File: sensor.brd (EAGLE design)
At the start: 64 x 64 mm, 27 parts, among them U1 NX1117C33Z, U2 NX1117CE50Z, U3 BMP180, U4 TSL2561

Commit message: Added some drill holes for mounting the PCB into a housing.
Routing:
- net N$2: track 25.7 -> 18.4 mm
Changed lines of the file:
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@@
 <wire x1="48.02125" y1="38.4575" x2="16.02125" y2="38.4575" width="0.254" layer="23"/>
 <wire x1="16.02125" y1="38.4575" x2="16.02125" y2="13.9575" width="0.254" layer="23"/>
+<hole x="3" y="32" drill="3.3"/>
+<hole x="61" y="32" drill="3.3"/>
 </plain>
 <attributes>
@@
 <contactref element="BAT2" pad="GND@1"/>
 <contactref element="BAT3" pad="PWR@1"/>
-<wire x1="57.146" y1="24" x2="62" y2="24" width="1.016" layer="1"/>
-<wire x1="62" y1="24" x2="62" y2="40" width="1.016" layer="1"/>
-<wire x1="62" y1="40" x2="57.146" y2="40" width="1.016" layer="1"/>
+<wire x1="57.146" y1="24" x2="58.34875" y2="24" width="1.016" layer="1"/>
+<wire x1="58.34875" y1="24" x2="58.34875" y2="40" width="1.016" layer="1"/>
+<wire x1="58.34875" y1="40" x2="57.146" y2="40" width="1.016" layer="1"/>
 </signal>
 <signal name="N$3">

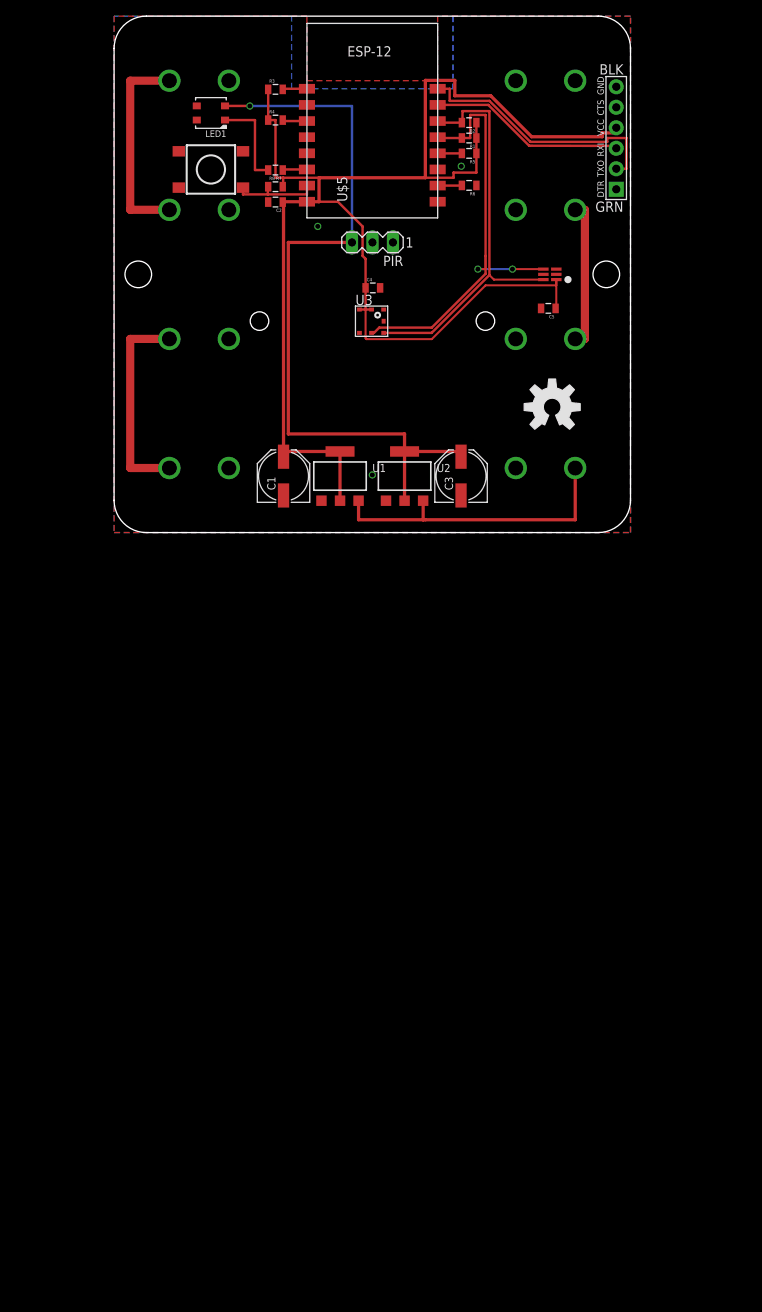
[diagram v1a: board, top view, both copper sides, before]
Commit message: lipo 18650 cell, TP4056 1A boost/charge controller
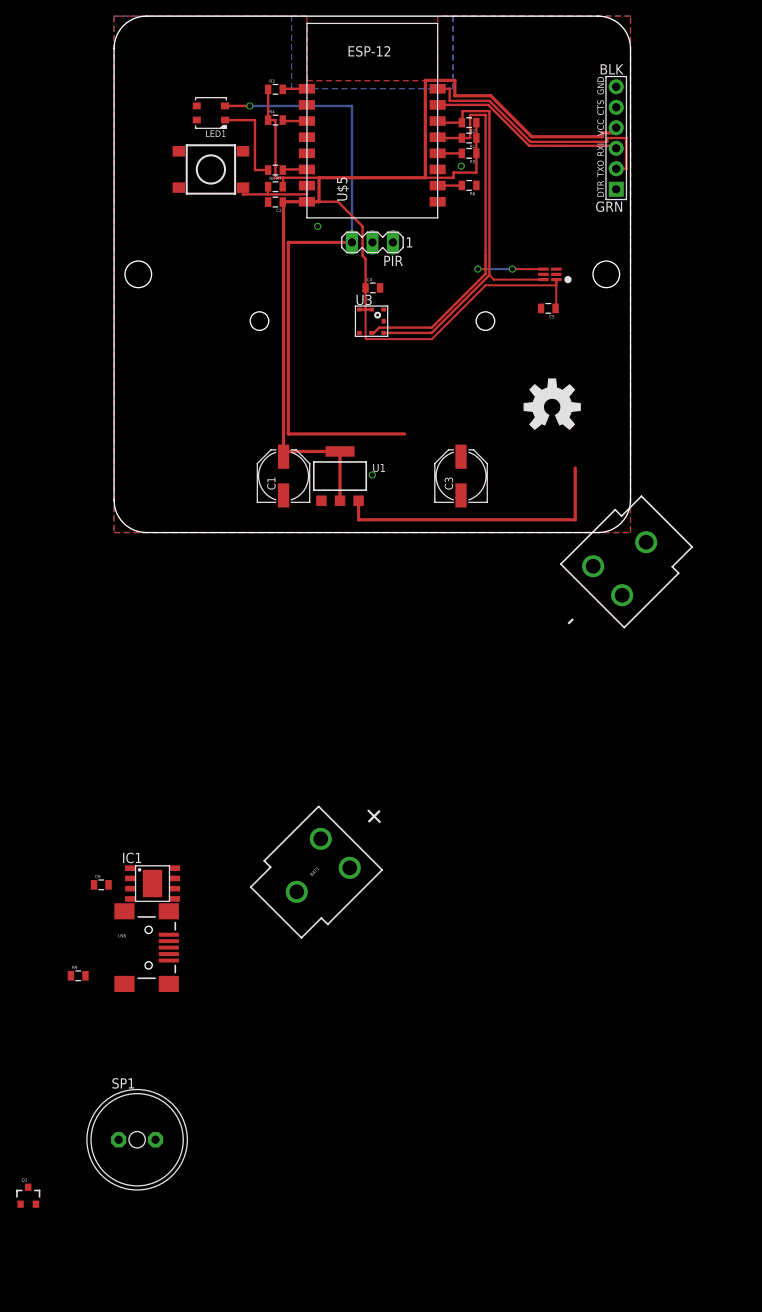
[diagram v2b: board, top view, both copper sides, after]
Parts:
- removed BAT2, BAT3, BAT4: (no value), SparkFun-Electromechanical:BATTERY-AA
- removed U2: NX1117CE50Z, nxp_60:SOT223
- added C6: 10uf, SparkFun-Capacitors:0805
- added IC1: TP4056, TP4056:SOP-8
- added Q1: (no value), SparkFun-DiscreteSemi:SOT23-3
- added R9: 122, SparkFun-Resistors:0805
- added SP1: SPEAKER/AL11P, adafruit:AL11P
- added U$6: USB-MINIB-5PIN, SparkFun-Connectors:USB-MINIB
- BAT1: device SparkFun-Electromechanical:BATTERY-AA -> SparkFun-Electromechanical:BATTERY_18650-HOLDER
- moved BAT1 33.2 mm to (44.3, -22.9), flipped to the top, turned to 45 degrees
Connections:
- removed net N$1: BAT1.GND@1, BAT2.PWR@1
- new net N$6: Q1.2, SP1.+
- new net SPKR: Q1.1
- new net USB_D+: U$6.D+
- new net USB_D-: U$6.D-
- net 5V: now also IC1.4, IC1.8, Q1.3, U$6.VBUS; no longer U2.2, U2.4
- net GND: now also BAT1.GND@1, C6.2, SP1.-, U$6.GND, U$6.MTN1, U$6.MTN2, U$6.MTN3, U$6.MTN4; no longer BAT4.GND@1, U2.1
- net N$2: now also IC1.1, IC1.3, R9.1; no longer BAT2.GND@1, BAT3.PWR@1
- net N$3: now also IC1.2, R9.2; no longer BAT3.GND@1, BAT4.PWR@1
- net V_BATT: now also C6.1, IC1.5; no longer U2.3
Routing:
- net N$3: track 25.7 -> 0.00 mm
- net N$1: track 25.7 -> 0.00 mm
- net N$2: track 18.4 -> 0.00 mm
- net 5V: track 94.6 -> 79.3 mm
- net V_BATT: track 38.0 -> 35.6 mm
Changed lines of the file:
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@@
 <attribute name="VOLTAGE" value="5.0V" x="28" y="7" size="1.778" layer="27" display="off"/>
 </element>
-<element name="U2" library="nxp_60" package="SOT223" value="NX1117CE50Z" x="36" y="7">
-<attribute name="TOLERANCE" value="1.25%" x="36" y="7" size="1.778" layer="27" display="off"/>
-<attribute name="12NC" value="" x="36" y="7" size="1.778" layer="27" display="off"/>
-<attribute name="VOLTAGE" value="5.0V" x="36" y="7" size="1.778" layer="27" display="off"/>
-</element>
-<element name="BAT1" library="SparkFun-Electromechanical" package="BATTERY-AA" value="" x="32" y="8" rot="MR0"/>
-<element name="BAT2" library="SparkFun-Electromechanical" package="BATTERY-AA" value="" x="32" y="24" rot="MR180"/>
-<element name="BAT3" library="SparkFun-Electromechanical" package="BATTERY-AA" value="" x="32" y="40" rot="MR0"/>
-<element name="BAT4" library="SparkFun-Electromechanical" package="BATTERY-AA" value="" x="32" y="56" rot="MR180"/>
 <element name="JP2" library="SparkFun-Connectors" package="FTDI_DEVICE_SIDE" value="FTDI_DEVICE" x="62.23" y="48.895" rot="R90"/>
 <element name="S1" library="SparkFun-Electromechanical" package="TACTILE_SWITCH_TALL" value="SWITCH-MOMENTARY-2SMD-4" x="12" y="45">
@@
 <element name="U4" library="microbuilder" package="TSL2561_FN" value="TSL2561" x="54" y="32" rot="R180"/>
 <element name="C5" library="SparkFun-Capacitors" package="0805" value="0.1uf" x="53.81625" y="27.78125" rot="R180"/>
+<element name="BAT1" library="SparkFun-Electromechanical" package="BATTERY_18650-HOLDER" value="" x="44.29125" y="-22.86" rot="R45"/>
+<element name="IC1" library="TP4056" package="SOP-8" value="TP4056" x="4.7625" y="-43.4975"/>
+<element name="C6" library="SparkFun-Capacitors" package="0805" value="10uf" x="-1.5875" y="-43.65625"/>
+<element name="U$6" library="SparkFun-Connectors" package="USB-MINIB" value="USB-MINIB-5PIN" x="4.28625" y="-51.435"/>
+<element name="R9" library="SparkFun-Resistors" package="0805" value="122" x="-4.445" y="-54.9275"/>
+<element name="SP1" library="adafruit" package="AL11P" value="SPEAKER/AL11P" x="2.8575" y="-75.2475"/>
+<element name="Q1" library="SparkFun-DiscreteSemi" package="SOT23-3" value="" x="-10.63625" y="-82.2325">
+<attribute name="PROD_ID" value="TRANS-08049" x="-10.63625" y="-82.2325" size="1.778" layer="27" display="off"/>
+</element>
 </elements>
 <signals>
@@
 <contactref element="R6" pad="1"/>
 <contactref element="LED1" pad="4"/>
-<contactref element="U2" pad="1"/>
 <contactref element="C3" pad="-"/>
 <contactref element="PIR" pad="1"/>
@@
 <vertex x="64" y="0"/>
 </polygon>
-<contactref element="BAT4" pad="GND@1"/>
 <contactref element="JP2" pad="P$6"/>
 <contactref element="S1" pad="B2"/>
@@
 <contactref element="U4" pad="ADR"/>
 <contactref element="C5" pad="2"/>
+<contactref element="BAT1" pad="GND@1"/>
+<contactref element="C6" pad="2"/>
+<contactref element="U$6" pad="MTN2"/>
+<contactref element="U$6" pad="MTN3"/>
+<contactref element="U$6" pad="MTN1"/>
+<contactref element="U$6" pad="MTN4"/>
+<contactref element="U$6" pad="GND"/>
+<contactref element="SP1" pad="-"/>
+<wire x1="1.28625" y1="-55.935" x2="0.5715" y2="-75.2475" width="0" layer="19" extent="1-1"/>
+<wire x1="6.78625" y1="-55.935" x2="1.28625" y2="-55.935" width="0" layer="19" extent="1-1"/>
+<wire x1="6.78625" y1="-53.035" x2="6.78625" y2="-55.935" width="0" layer="19" extent="1-1"/>
+<wire x1="6.78625" y1="-46.935" x2="6.78625" y2="-53.035" width="0" layer="19" extent="1-1"/>
+<wire x1="1.28625" y1="-46.935" x2="6.78625" y2="-46.935" width="0" layer="19" extent="1-1"/>
+<wire x1="-0.6875" y1="-43.65625" x2="1.28625" y2="-46.935" width="0" layer="19" extent="1-1"/>
+<wire x1="21" y1="4.6" x2="-0.6875" y2="-43.65625" width="0" layer="19" extent="1-1"/>
+<wire x1="65.94144375" y1="-1.195659375" x2="43" y2="4.6" width="0" layer="19" extent="1-1"/>
 </signal>
 <signal name="TX">
@@
 <contactref element="LED1" pad="2"/>
 <contactref element="C3" pad="+"/>
-<contactref element="U2" pad="4"/>
-<contactref element="U2" pad="2"/>
 <contactref element="PIR" pad="3"/>
-<wire x1="36" y1="3.95" x2="36" y2="10.05" width="0.4064" layer="1"/>
-<wire x1="36" y1="10.05" x2="43" y2="10.05" width="0.4064" layer="1"/>
 <wire x1="43" y1="10.05" x2="43" y2="9.4" width="0.4064" layer="1"/>
-<wire x1="36" y1="10.05" x2="36" y2="12.22375" width="0.4064" layer="1"/>
 <wire x1="36" y1="12.22375" x2="21.59" y2="12.22375" width="0.4064" layer="1"/>
 <wire x1="21.59" y1="12.22375" x2="21.59" y2="35.9575" width="0.4064" layer="1"/>
@@
 <wire x1="16.8275" y1="52.86375" x2="29.48125" y2="52.86375" width="0.3048" layer="16"/>
 <wire x1="29.48125" y1="52.86375" x2="29.48125" y2="35.9575" width="0.3048" layer="16"/>
+<contactref element="U$6" pad="VBUS"/>
+<contactref element="IC1" pad="8"/>
+<contactref element="IC1" pad="4"/>
+<contactref element="Q1" pad="3"/>
+<wire x1="6.78625" y1="-49.835" x2="-10.63625" y2="-81.1325" width="0" layer="19" extent="1-1"/>
+<wire x1="2.0125" y1="-45.4025" x2="6.78625" y2="-49.835" width="0" layer="19" extent="1-1"/>
+<wire x1="7.5125" y1="-41.5925" x2="2.0125" y2="-45.4025" width="0" layer="19" extent="1-1"/>
+<wire x1="21.59" y1="12.22375" x2="7.5125" y2="-41.5925" width="0" layer="19" extent="1-1"/>
+<wire x1="43" y1="10.05" x2="36" y2="12.22375" width="0" layer="19" extent="1-1"/>
 </signal>
 <signal name="LED_DI">
@@
 <contactref element="PIR" pad="2"/>
 </signal>
-<signal name="N$1">
-<contactref element="BAT1" pad="GND@1"/>
-<contactref element="BAT2" pad="PWR@1"/>
-<wire x1="6.854" y1="24" x2="2" y2="24" width="1.016" layer="1"/>
-<wire x1="2" y1="24" x2="2" y2="8" width="1.016" layer="1"/>
-<wire x1="6.854" y1="8" x2="2" y2="8" width="1.016" layer="1"/>
-</signal>
-<signal name="N$2">
-<contactref element="BAT2" pad="GND@1"/>
-<contactref element="BAT3" pad="PWR@1"/>
-<wire x1="57.146" y1="24" x2="58.34875" y2="24" width="1.016" layer="1"/>
-<wire x1="58.34875" y1="24" x2="58.34875" y2="40" width="1.016" layer="1"/>
-<wire x1="58.34875" y1="40" x2="57.146" y2="40" width="1.016" layer="1"/>
-</signal>
-<signal name="N$3">
-<contactref element="BAT3" pad="GND@1"/>
-<contactref element="BAT4" pad="PWR@1"/>
-<wire x1="6.854" y1="40" x2="2" y2="40" width="1.016" layer="1"/>
-<wire x1="2" y1="40" x2="2" y2="56" width="1.016" layer="1"/>
-<wire x1="6.854" y1="56" x2="2" y2="56" width="1.016" layer="1"/>
-</signal>
 <signal name="V_BATT">
-<contactref element="BAT1" pad="PWR@1"/>
-<contactref element="U2" pad="3"/>
 <contactref element="U1" pad="3"/>
 <wire x1="30.3" y1="3.95" x2="30.3" y2="1.5875" width="0.4064" layer="1"/>
-<wire x1="30.3" y1="1.5875" x2="38.3" y2="1.5875" width="0.4064" layer="1"/>
-<wire x1="38.57625" y1="1.5875" x2="57.15" y2="1.5875" width="0.4064" layer="1"/>
+<wire x1="30.3" y1="1.5875" x2="57.15" y2="1.5875" width="0.4064" layer="1"/>
 <wire x1="57.15" y1="1.5875" x2="57.15" y2="8" width="0.4064" layer="1"/>
-<wire x1="57.15" y1="8" x2="57.146" y2="8" width="0.4064" layer="1"/>
-<wire x1="38.3" y1="3.95" x2="38.3" y2="1.5875" width="0.4064" layer="1"/>
-<wire x1="38.3" y1="1.5875" x2="38.57625" y2="1.5875" width="0.4064" layer="1"/>
+<contactref element="BAT1" pad="PWR@1"/>
+<contactref element="IC1" pad="5"/>
+<contactref element="C6" pad="1"/>
+<wire x1="7.5125" y1="-45.4025" x2="-2.4875" y2="-43.65625" width="0" layer="19" extent="1-1"/>
+<wire x1="22.641053125" y1="-44.5243375" x2="7.5125" y2="-45.4025" width="0" layer="19" extent="1-1"/>
+<wire x1="30.3" y1="1.5875" x2="22.641053125" y2="-44.5243375" width="0" layer="19" extent="1-1"/>
 </signal>
 <signal name="INT">
 <contactref element="U4" pad="INT"/>
 </signal>
+<signal name="USB_D-">
+<contactref element="U$6" pad="D-"/>
+</signal>
+<signal name="USB_D+">
+<contactref element="U$6" pad="D+"/>
+</signal>
+<signal name="N$2">
+<contactref element="IC1" pad="3"/>
+<contactref element="R9" pad="1"/>
+<contactref element="IC1" pad="1"/>
+<wire x1="2.0125" y1="-44.1325" x2="-5.345" y2="-54.9275" width="0" layer="19" extent="1-1"/>
+<wire x1="2.0125" y1="-41.5925" x2="2.0125" y2="-44.1325" width="0" layer="19" extent="1-1"/>
+</signal>
+<signal name="N$3">
+<contactref element="R9" pad="2"/>
+<contactref element="IC1" pad="2"/>
+<wire x1="2.0125" y1="-42.8625" x2="-3.545" y2="-54.9275" width="0" layer="19" extent="1-1"/>
+</signal>
+<signal name="N$6">
+<contactref element="Q1" pad="2"/>
+<contactref element="SP1" pad="+"/>
+<wire x1="5.1435" y1="-75.2475" x2="-9.68625" y2="-83.2325" width="0" layer="19" extent="1-1"/>
+</signal>
+<signal name="SPKR">
+<contactref element="Q1" pad="1"/>
+</signal>
 </signals>

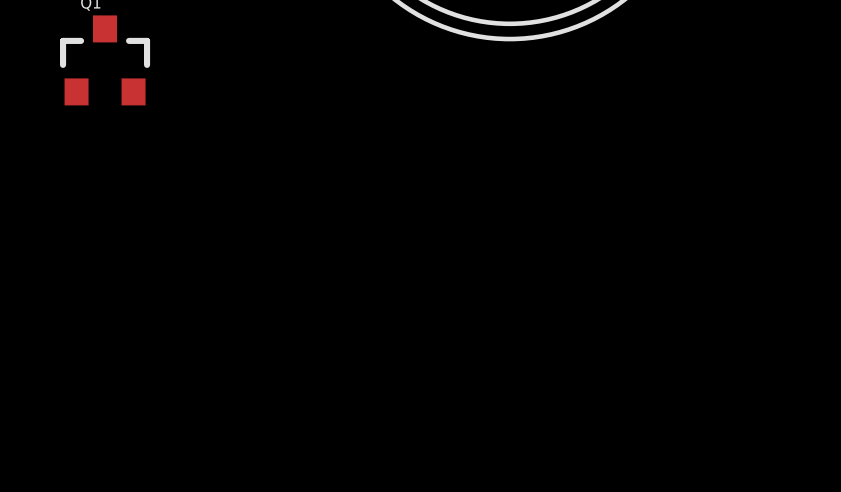
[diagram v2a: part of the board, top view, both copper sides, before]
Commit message: Move schematic around to be more pleasing, add i2c header as per @badspyro's request.
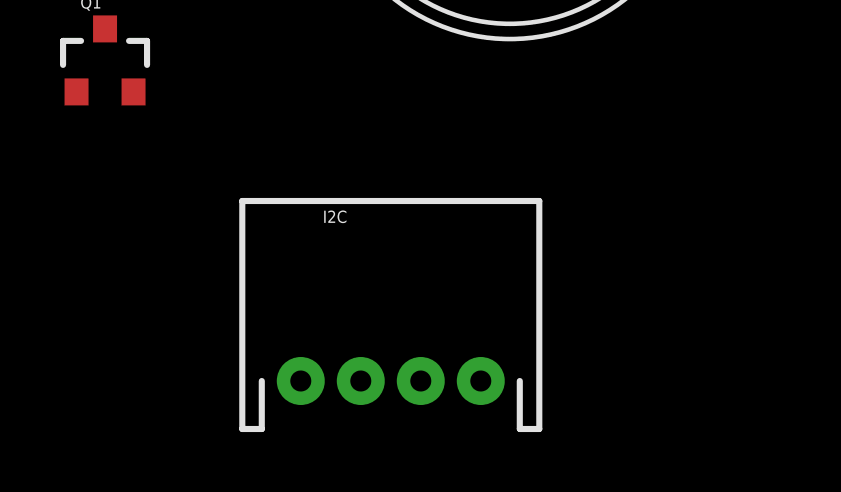
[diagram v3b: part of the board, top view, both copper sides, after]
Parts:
- added I2C: (no value), SparkFun-Connectors:JST-4-PTH
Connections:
- net 5V: now also I2C.4
- net GND: now also I2C.1
- net SCL: now also I2C.3
- net SDA: now also I2C.2
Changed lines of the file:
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@@
 <attribute name="PROD_ID" value="TRANS-08049" x="-10.63625" y="-82.2325" size="1.778" layer="27" display="off"/>
+</element>
+<element name="I2C" library="SparkFun-Connectors" package="JST-4-PTH" value="" x="-1.11125" y="-92.86875">
+<attribute name="SKU" value="PRT-09916" x="-1.11125" y="-92.86875" size="1.778" layer="27" display="off"/>
 </element>
 </elements>
@@
 <contactref element="U$6" pad="GND"/>
 <contactref element="SP1" pad="-"/>
+<contactref element="I2C" pad="1"/>
+<wire x1="0.5715" y1="-75.2475" x2="-4.11125" y2="-92.86875" width="0" layer="19" extent="1-1"/>
 <wire x1="1.28625" y1="-55.935" x2="0.5715" y2="-75.2475" width="0" layer="19" extent="1-1"/>
 <wire x1="6.78625" y1="-55.935" x2="1.28625" y2="-55.935" width="0" layer="19" extent="1-1"/>
@@
 <wire x1="53.2" y1="31.35" x2="47.0725" y2="31.35" width="0.254" layer="1"/>
 <wire x1="47.0725" y1="31.35" x2="46.51375" y2="31.90875" width="0.254" layer="1"/>
+<contactref element="I2C" pad="2"/>
+<wire x1="33.40875" y1="24.74375" x2="-2.11125" y2="-92.86875" width="0" layer="19" extent="1-1"/>
 </signal>
 <signal name="SCL">
@@
 <wire x1="45.085" y1="32.65" x2="46.0375" y2="32.65" width="0.254" layer="1"/>
 <wire x1="46.0375" y1="32.65" x2="46.0375" y2="34.29" width="0.254" layer="1"/>
+<contactref element="I2C" pad="3"/>
+<wire x1="31.90875" y1="24.74375" x2="-0.11125" y2="-92.86875" width="0" layer="19" extent="1-1"/>
 </signal>
 <signal name="GPIO0">
@@
 <contactref element="IC1" pad="4"/>
 <contactref element="Q1" pad="3"/>
+<contactref element="I2C" pad="4"/>
+<wire x1="-10.63625" y1="-81.1325" x2="1.88875" y2="-92.86875" width="0" layer="19" extent="1-1"/>
 <wire x1="6.78625" y1="-49.835" x2="-10.63625" y2="-81.1325" width="0" layer="19" extent="1-1"/>
 <wire x1="2.0125" y1="-45.4025" x2="6.78625" y2="-49.835" width="0" layer="19" extent="1-1"/>

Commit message: Redo.. but oops.
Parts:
- removed C3: (no value), SparkFun-Capacitors:PANASONIC_D
- removed LED1: WS2812B3535, adafruit:LED3535
- removed R7: 470, SparkFun-Resistors:0805
- removed R8: 10k, SparkFun-Resistors:0805
- added C7: 0.1uF, rcl:C0805
- added C8, C9: 22pf, rcl:C0805
- added LED2: LED-TRICOLOR-5050NO_IC, SparkFun-LED:LED-TRICOLOR-5050
- added U$11: CH340G, CH340G-USB-SERIAL:SOIC16
- added Y1: 12mhz, SparkFun-FreqCtrl:HC49UP
- C6: value 10uf -> (none); device SparkFun-Capacitors:0805 -> SparkFun-Capacitors:PANASONIC_D
- moved Q1 143.9 mm to (58.6, 44.0), turned to 90 degrees
- moved SP1 134.1 mm to (68.0, 42.0), turned to 135 degrees
- moved I2C 109.3 mm to (48.0, 4.76), turned to 180 degrees
- moved C6 90.9 mm to (65.7, 17.5), turned to 180 degrees
- moved R9 87.8 mm to (50.2, 13.8), turned to 90 degrees
- moved IC1 76.3 mm to (55.1, 13.8)
- moved U$6 58.6 mm to (21.6, 4.60), turned to 90 degrees
- moved JP2 50.3 mm to (11.9, 48.3), turned to 180 degrees
- moved C1 48.1 mm to (65.7, 24.7), turned to 180 degrees
- moved R3 46.4 mm to (50.0, 19.5), turned to 180 degrees
- moved R4 40.8 mm to (50.0, 23.5), turned to 180 degrees
- moved BAT1 34.4 mm to (38.0, 11.0), flipped to the bottom, turned to 0 degrees
- moved R2 32.7 mm to (25.9, 23.7), turned to 0 degrees
- moved U1 32.6 mm to (56.7, 22.4)
- moved R1 29.6 mm to (25.9, 25.6), turned to 0 degrees
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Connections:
- removed net LED_DI: LED1.1, R7.2
- removed net N$2: IC1.1, IC1.3, R9.1
- removed net SENSE: PIR.2
- removed net SPKR: Q1.1
- new net OSCI: C8.1, U$11.7, Y1.1
- new net OSCO: C9.1, U$11.8, Y1.2
- net 3.3V: now also C7.1, I2C.4, PIR.3, Q1.3, U$11.16, U$11.4; no longer R8.2
- net 5V: no longer C3.+, I2C.4, LED1.2, PIR.3, Q1.3
- net GND: now also C6.-, C7.2, C8.2, C9.2, IC1.1, IC1.3, LED2.4, LED2.5, LED2.6, R9.1, U$11.1; no longer C3.-, C6.2, LED1.4
- net GPIO0: now also S1.A2
- net GPIO12: now also LED2.3; no longer R7.1
- net GPIO13: now also Q1.1; no longer R8.1, S1.A2
- net GPIO14: now also LED2.2
- net GPIO16: now also LED2.1
- net GPIO2: now also PIR.2
- net RX: now also U$11.2
- net TX: now also U$11.3
- net USB_D+: now also U$11.5
- net USB_D-: now also U$11.6
- net V_BATT: now also C6.+; no longer C6.1
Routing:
- net GPIO16: track 0.00 -> 39.5 mm, vias 0 -> 2
- net GPIO14: track 0.00 -> 38.9 mm, vias 0 -> 2
- net GPIO12: track 3.07 -> 39.3 mm, vias 0 -> 2
- net SDA: track 51.4 -> 87.3 mm, vias 0 -> 1
- net SCL: track 56.5 -> 90.4 mm, vias 2 -> 1
- net GPIO2: track 0.00 -> 25.9 mm, vias 0 -> 1
- net RX: track 24.5 -> 49.0 mm, vias 0 -> 1
- net TX: track 32.6 -> 52.5 mm, vias 0 -> 1
- net GPIO13: track 11.1 -> 28.5 mm, vias 0 -> 2
- net OSCO: track 0.00 -> 14.8 mm
- net USB_D+: track 0.00 -> 12.1 mm
- net USB_D-: track 0.00 -> 11.7 mm
- net LED_DI: track 11.5 -> 0.00 mm
- net V_BATT: track 35.6 -> 24.4 mm
- net 5V: track 79.3 -> 68.4 mm, vias 1 -> 0
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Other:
- board size 64 x 64 mm -> 76 x 50 mm
